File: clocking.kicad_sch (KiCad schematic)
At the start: 46 parts, among them U2 TG5032CGN, U3 LMK05318BRGZR, U31 TMP117xxDRV

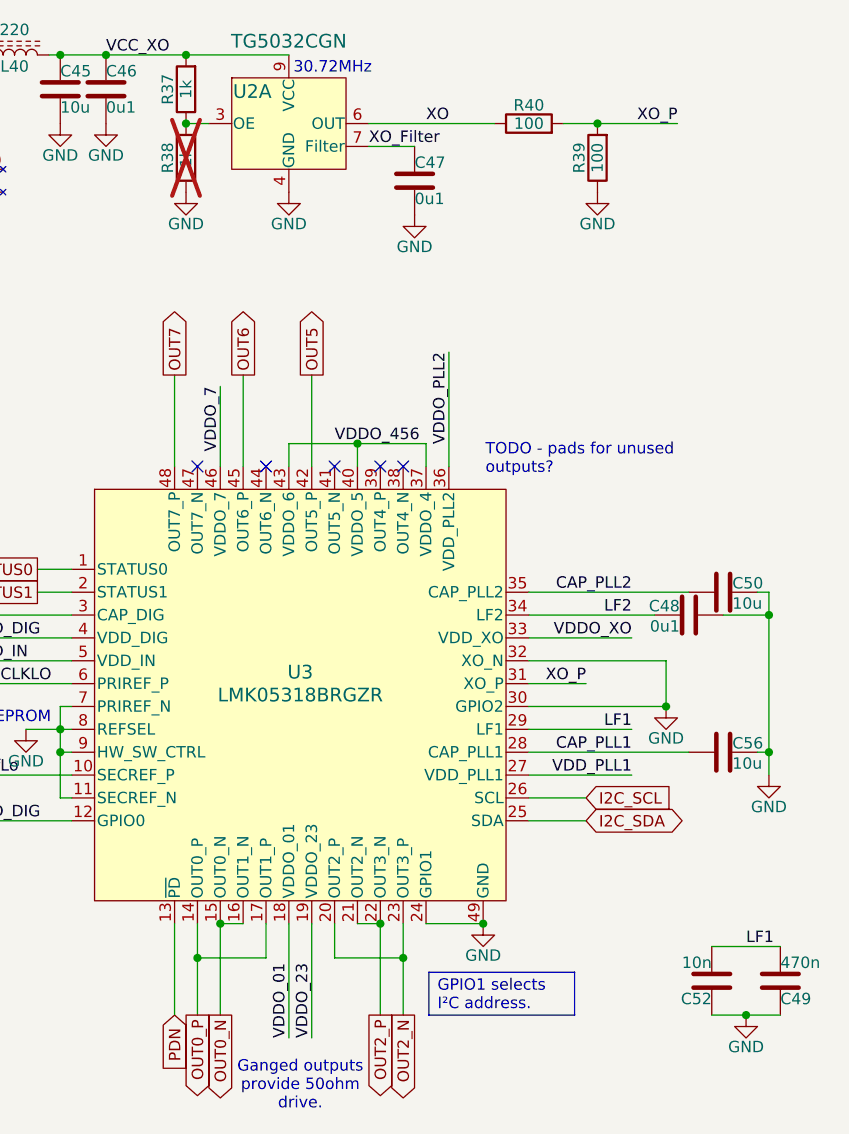
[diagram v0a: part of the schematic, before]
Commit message: DRC clean-up.  Only silk-screen noise left.
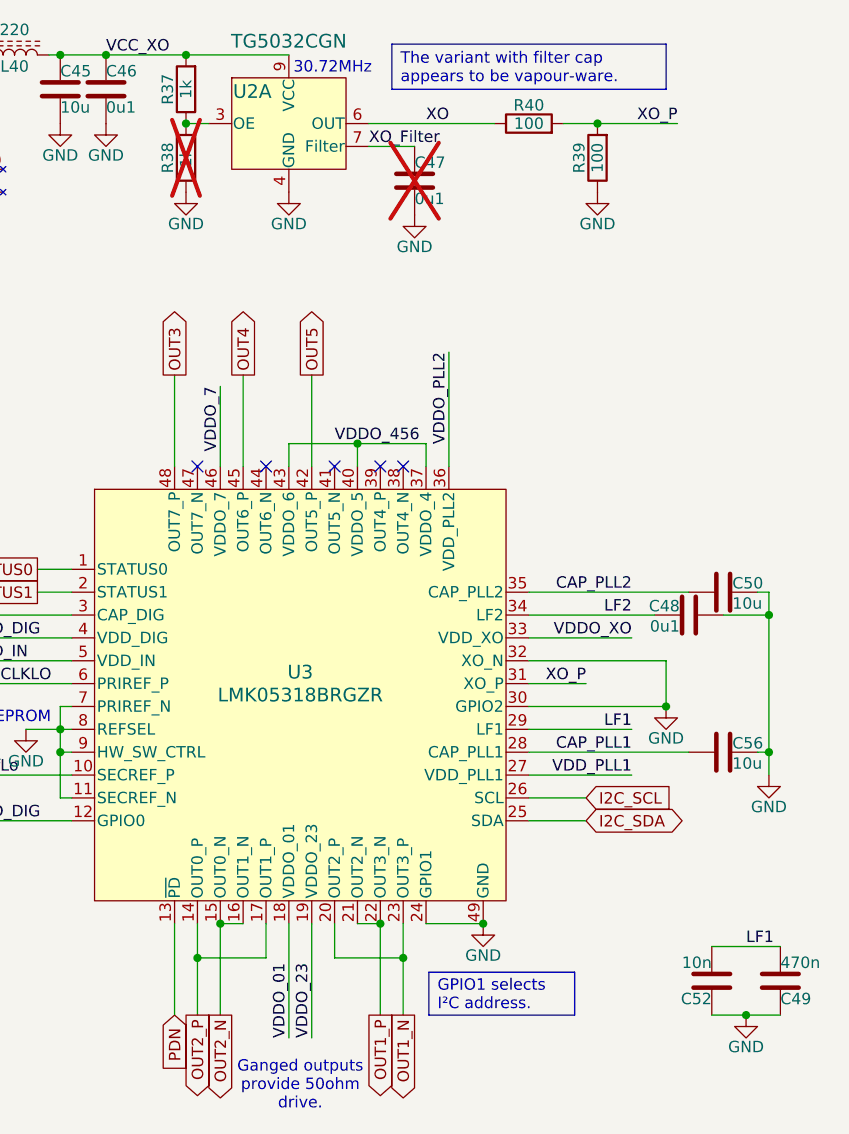
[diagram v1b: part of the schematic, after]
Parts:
- C47: now not fitted
- C49: footprint Capacitor_THT:C_Rect_L7.2mm_W3.5mm_P5.00mm_FKS2_FKP2_MKS2_MKP2 -> Capacitor_SMD:C_1206_3216Metric
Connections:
- net OUT0_N is gone; now on net OUT2_N: U3.15 (OUT0_N), U3.16 (OUT1_N)
- net OUT0_P is gone; now on net OUT2_P: U3.14 (OUT0_P), U3.17 (OUT1_P)
- net OUT2_N: no longer U3.20 (OUT2_P), U3.23 (OUT3_P)
- net OUT2_P: no longer U3.21 (OUT2_N), U3.22 (OUT3_N)
- net OUT6 renamed OUT4
- net OUT7 renamed OUT3
- new net OUT1_N: U3.20 (OUT2_P), U3.23 (OUT3_P)
- new net OUT1_P: U3.21 (OUT2_N), U3.22 (OUT3_N)
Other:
- note removed: "TODO - pads for unused outputs?"
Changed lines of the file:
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@@
 		)
 	)
-	(text "TODO - pads for unused\noutputs?"
-		(exclude_from_sim no)
-		(at 222.504 77.978 0)
-		(effects
-			(font
-				(size 1.27 1.27)
-			)
-			(justify left)
-		)
-	)
 	(text "Ganged outputs\nprovide 50ohm\ndrive.\n"
 		(exclude_from_sim no)
@@
 		)
 	)
+	(text_box "The variant with filter cap appears to be vapour-ware."
+		(exclude_from_sim no)
+		(at 212.1153 31.8079 0)
+		(size 30.4547 5.0221)
+		(margins 0.9525 0.9525 0.9525 0.9525)
+		(stroke
+			(width 0)
+			(type solid)
+		)
+		(fill
+			(type none)
+		)
+		(effects
+			(font
+				(size 1.27 1.27)
+			)
+			(justify left)
+		)
+	)
 	(junction
 		(at 69.85 93.98)
@@
 		)
 	)
-	(global_label "OUT2_P"
+	(global_label "OUT1_P"
 		(shape output)
 		(at 210.82 139.7 270)
@@
 		)
 	)
-	(global_label "OUT0_N"
+	(global_label "OUT2_N"
 		(shape output)
 		(at 193.04 139.7 270)
@@
 		)
 	)
-	(global_label "OUT6"
+	(global_label "OUT4"
 		(shape output)
 		(at 195.58 68.58 90)
@@
 		)
 	)
-	(global_label "OUT2_N"
+	(global_label "OUT1_N"
 		(shape output)
 		(at 213.36 139.7 270)
@@
 		)
 	)
-	(global_label "OUT0_P"
+	(global_label "OUT2_P"
 		(shape output)
 		(at 190.5 139.7 270)
@@
 		)
 	)
-	(global_label "OUT7"
+	(global_label "OUT3"
 		(shape output)
 		(at 187.96 68.58 90)
@@
 		(in_bom no)
 		(on_board yes)
-		(dnp no)
+		(dnp yes)
 		(property "Reference" "C47"
 			(at 214.63 45.72 0)
@@
 			)
 		)
-		(property "Footprint" "Capacitor_THT:C_Rect_L7.2mm_W3.5mm_P5.00mm_FKS2_FKP2_MKS2_MKP2"
+		(property "Footprint" "Capacitor_SMD:C_1206_3216Metric"
 			(at 256.2352 139.7 0)
 			(effects
@@
 			)
 		)
-		(property "Datasheet" "Film"
+		(property "Datasheet" "C0G"
 			(at 255.27 135.89 0)
 			(effects

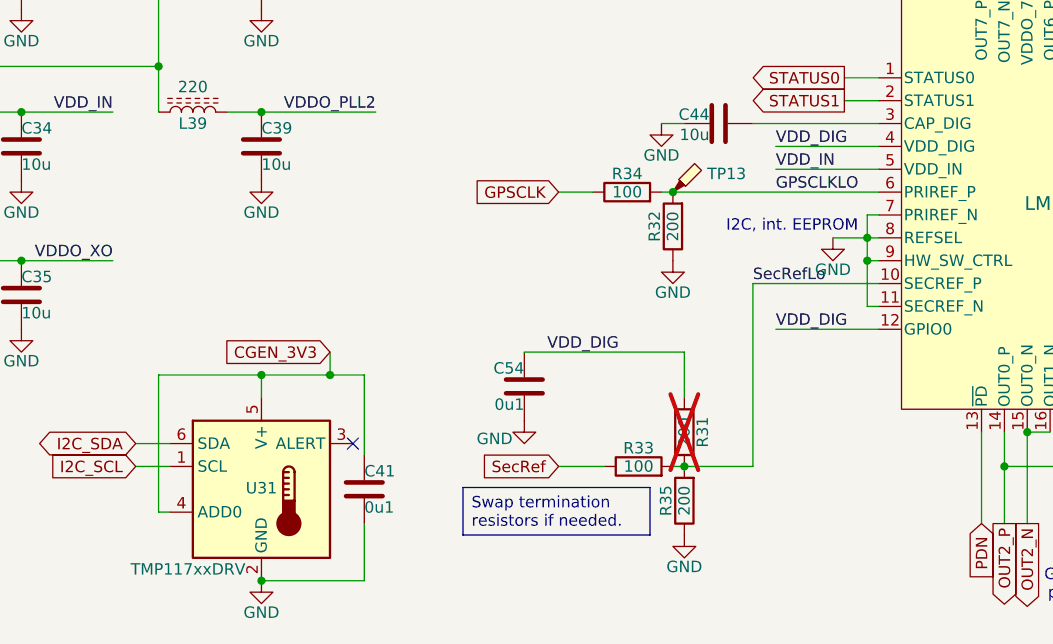
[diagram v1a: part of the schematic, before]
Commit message: Redo the secondary reference termination.
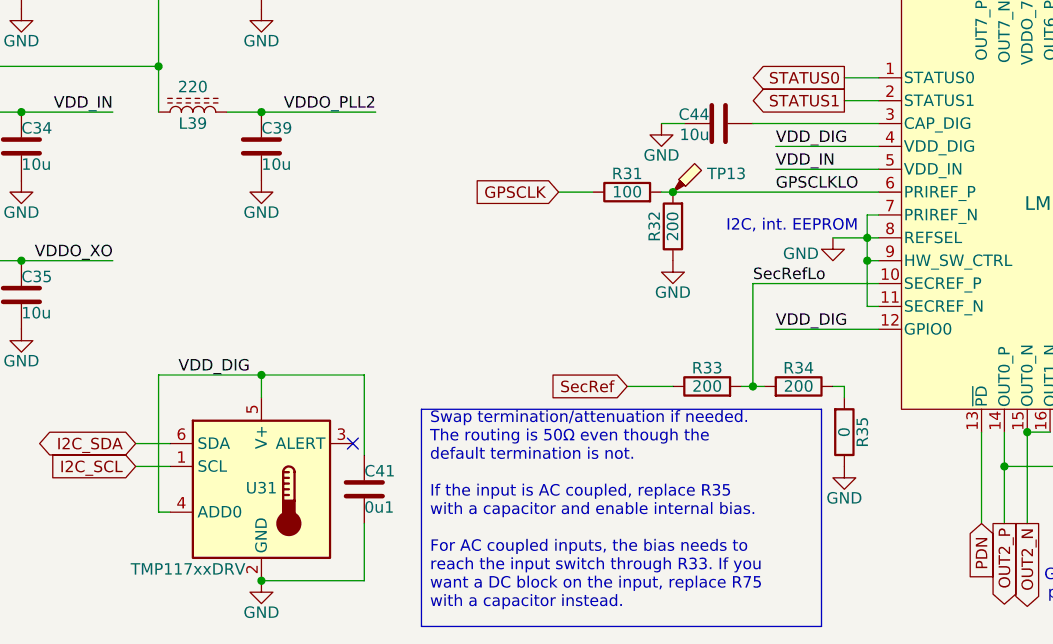
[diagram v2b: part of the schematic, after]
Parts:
- removed C54: 0u1, Capacitor_SMD:C_0402_1005Metric, symbol Device:C
- R33: value 100 -> 200; JLCPCB C22775 -> (none)
- R35: renamed from R31; value 200 -> 0; now fitted
- renumbered R34 to R31, R35 to R34
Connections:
- net CGEN_3V3: no longer C41.1, U31.4 (ADD0), U31.5 (V+)
- net GND: now also R35.1; no longer R34.1
- net SecRefLo: no longer R35.1
- net VDD_DIG: now also C41.1, U31.4 (ADD0), U31.5 (V+); no longer R35.2
- new net: R34.1, R35.2
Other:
- moved on the sheet: R33, R34

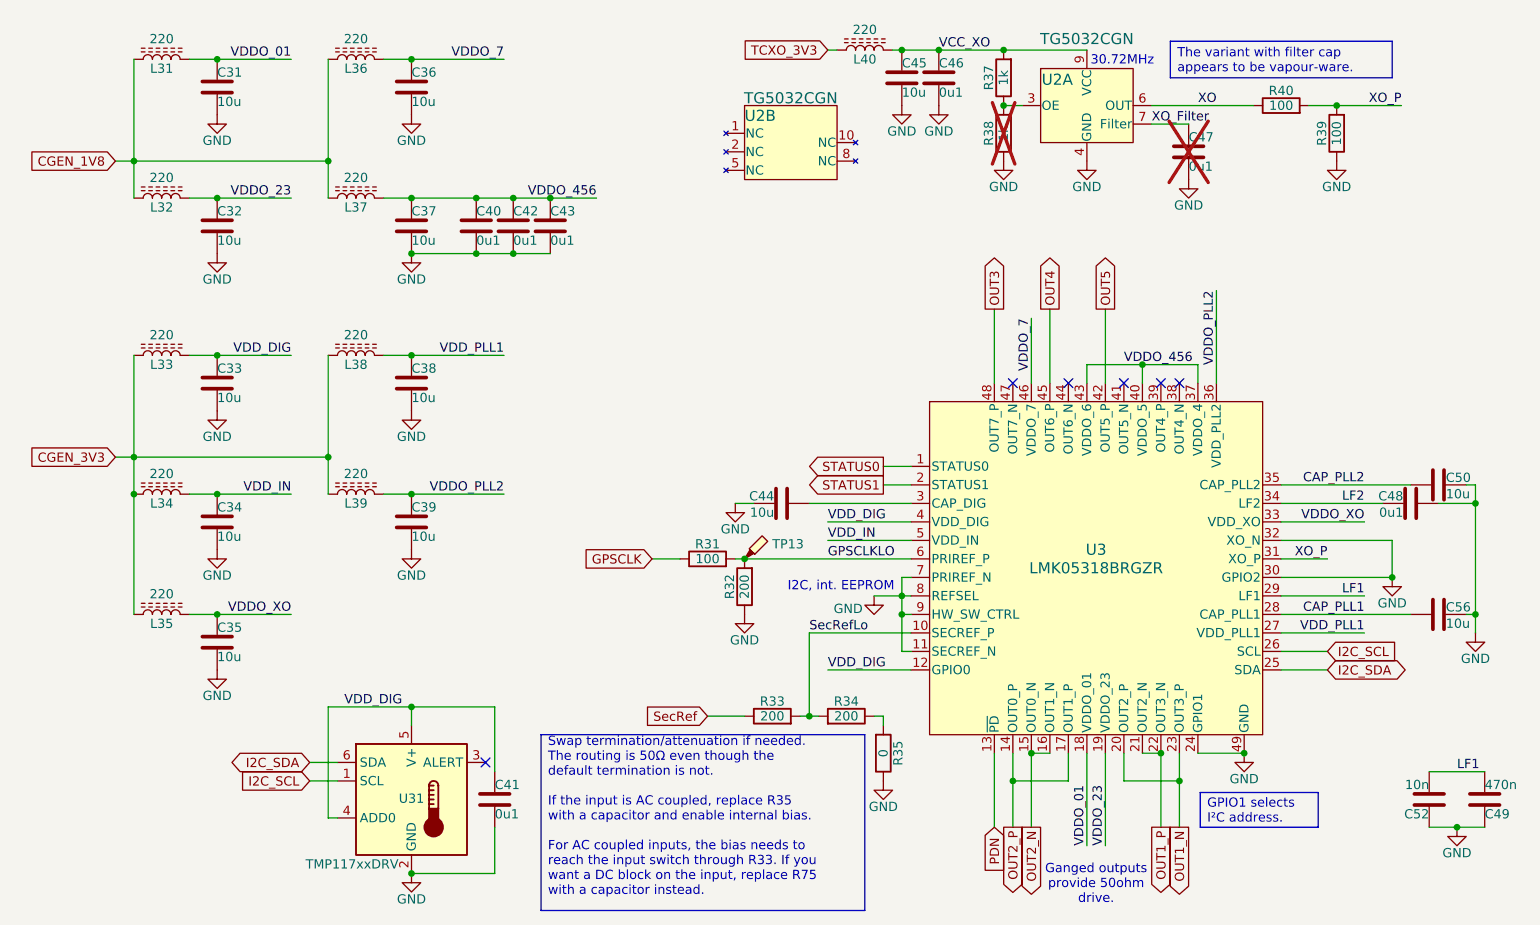
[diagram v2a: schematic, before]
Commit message: Squeeze in a connector to break out GPS.
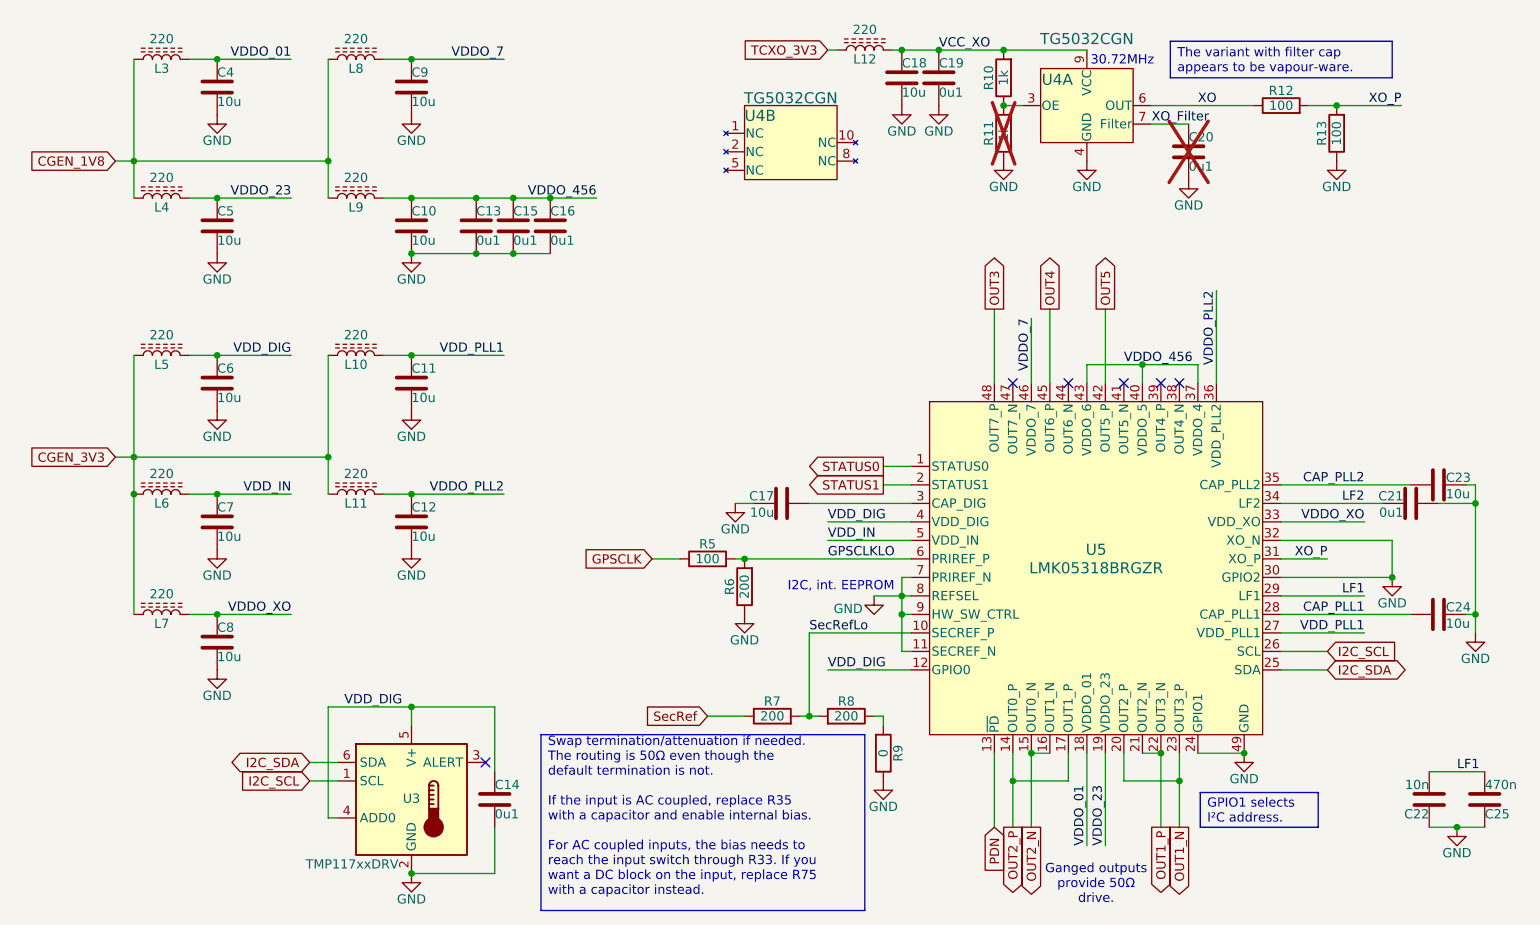
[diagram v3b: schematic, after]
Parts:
- removed TP13: TestPoint_Probe, Parts:TestPoint, symbol Connector:TestPoint_Probe
- renumbered C37 to C10, C38 to C11, C39 to C12, C40 to C13, C41 to C14, C42 to C15, C43 to C16, C44 to C17, C45 to C18, C46 to C19, C47 to C20, C48 to C21, C52 to C22, C50 to C23, C56 to C24, C49 to C25, C31 to C4, C32 to C5, C33 to C6, C34 to C7, C35 to C8, C36 to C9, L38 to L10, L39 to L11, L40 to L12, L31 to L3, L32 to L4, L33 to L5, L34 to L6, L35 to L7, L36 to L8, L37 to L9, R37 to R10, R38 to R11, R40 to R12, R39 to R13, R31 to R5, R32 to R6, R33 to R7, R34 to R8, R35 to R9, U31 to U3, U2 to U4, U3 to U5
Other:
- note added: "Ganged outputs provide 50Ω drive."
- note removed: "Ganged outputs provide 50ohm drive."
